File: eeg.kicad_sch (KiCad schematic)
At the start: 6 parts, among them J1 Conn_01x03, J2 Conn_01x04, U2 BMI270

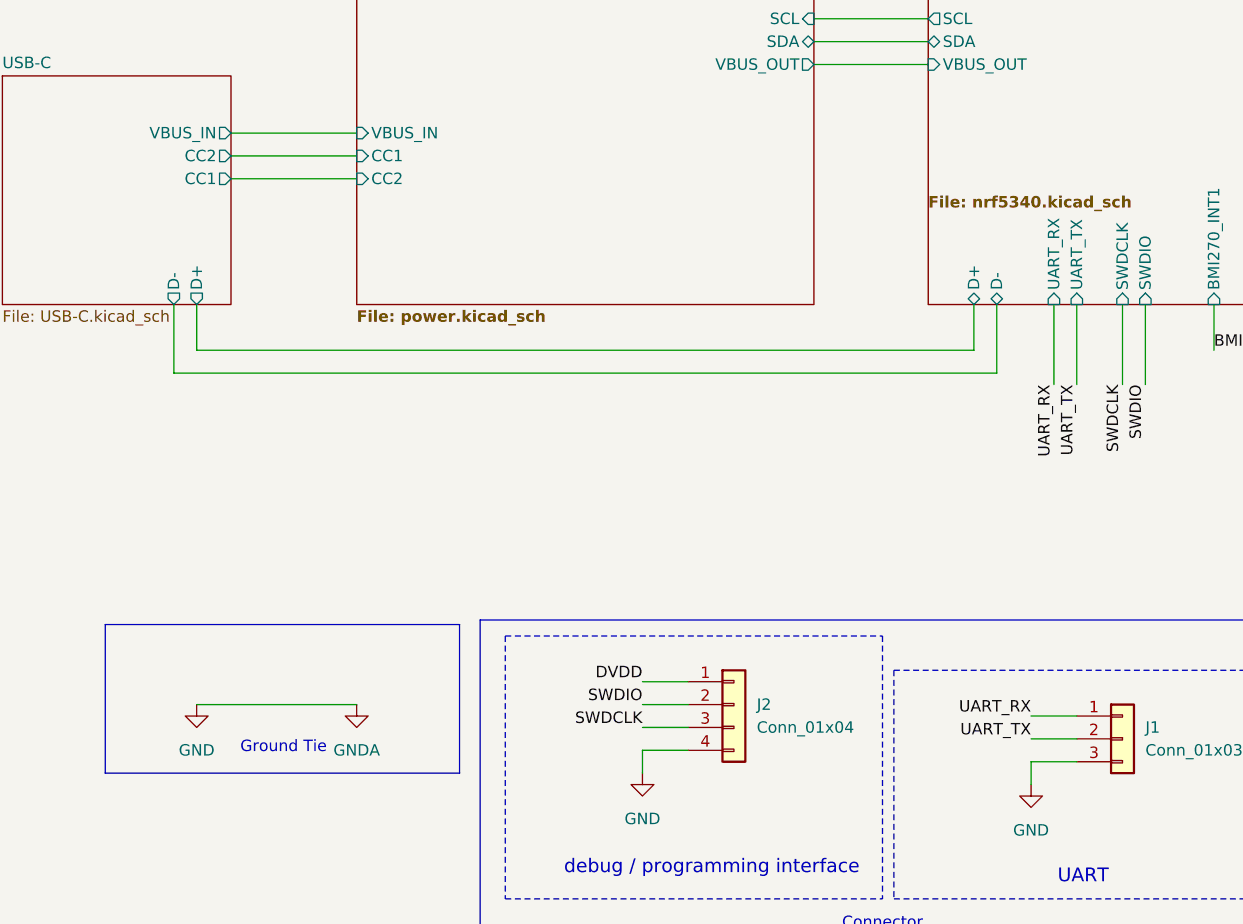
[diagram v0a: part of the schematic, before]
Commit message: Feat: 개발보드 버전으로 PCB 변경
수정사항

단가 감소
- PCB Board size up (50x50)
- blind via 제거 (전체 레이아웃 수정)
- AVDD 전력평면 추가
- ADS1299 안쓰는핀 GND
- ADS1299 배치 변경 (Layout Reference 적용)

개발보드만 적용사항
- Pin Header size up 1.27 → 2.54mm
- PCB Size 50x50(mm)
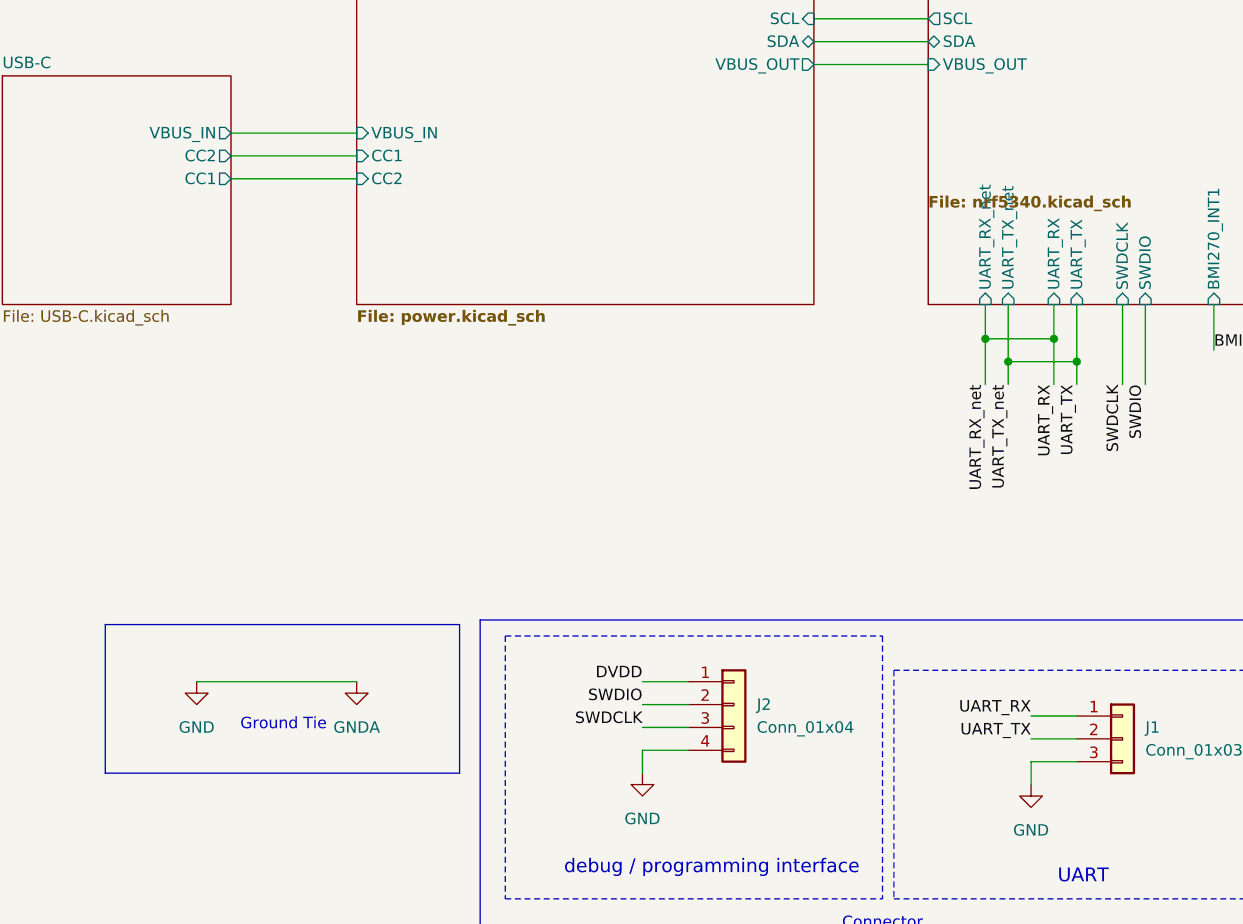
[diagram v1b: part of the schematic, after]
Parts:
- J1: footprint Connector_PinHeader_1.27mm:PinHeader_1x03_P1.27mm_Vertical -> Connector_PinHeader_2.54mm:PinHeader_1x03_P2.54mm_Vertical
- J2: footprint Connector_PinHeader_1.27mm:PinHeader_1x04_P1.27mm_Vertical -> Connector_PinHeader_2.54mm:PinHeader_1x04_P2.54mm_Vertical
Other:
- sheet USB-C ports: added none; removed D+, D-
- sheet nrf5340 ports: added UART_RX_net, UART_TX_net; removed D+, D-

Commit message: Doc: Gerber Data V0.2(dev)
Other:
- sheet nrf5340 ports: added none; removed UART_RX_net, UART_TX_net
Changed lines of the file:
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@@
 	(paper "A4")
-	(junction
-		(at 158.75 95.25)
-		(diameter 0)
-		(color 0 0 0 0)
-	)
 	(junction
 		(at 254 114.3)
@@
 	)
 	(junction
-		(at 168.91 97.79)
-		(diameter 0)
-		(color 0 0 0 0)
-	)
-	(junction
 		(at 266.7 111.76)
 		(diameter 0)
@@
 	)
 	(junction
-		(at 161.29 97.79)
-		(diameter 0)
-		(color 0 0 0 0)
-	)
-	(junction
-		(at 166.37 95.25)
-		(diameter 0)
-		(color 0 0 0 0)
-	)
-	(junction
 		(at 255.27 147.32)
 		(diameter 0)
@@
 		)
 	)
-	(wire
-		(pts
-			(xy 161.29 97.79) (xy 168.91 97.79)
-		)
-		(stroke
-			(width 0)
-			(type default)
-		)
-	)
-	(wire
-		(pts
-			(xy 158.75 100.33) (xy 158.75 95.25)
-		)
-		(stroke
-			(width 0)
-			(type default)
-		)
-	)
 	(polyline
 		(pts
@@
 	(wire
 		(pts
-			(xy 168.91 97.79) (xy 168.91 100.33)
-		)
-		(stroke
-			(width 0)
-			(type default)
-		)
-	)
-	(wire
-		(pts
 			(xy 176.53 91.44) (xy 176.53 100.33)
 		)
@@
 	(wire
 		(pts
-			(xy 161.29 100.33) (xy 161.29 97.79)
-		)
-		(stroke
-			(width 0)
-			(type default)
-		)
-	)
-	(wire
-		(pts
 			(xy 210.82 82.55) (xy 215.9 82.55)
 		)
@@
 	(wire
 		(pts
-			(xy 158.75 95.25) (xy 166.37 95.25)
-		)
-		(stroke
-			(width 0)
-			(type default)
-		)
-	)
-	(wire
-		(pts
 			(xy 240.03 36.83) (xy 240.03 40.64)
 		)
@@
 	(wire
 		(pts
-			(xy 166.37 95.25) (xy 166.37 100.33)
-		)
-		(stroke
-			(width 0)
-			(type default)
-		)
-	)
-	(wire
-		(pts
 			(xy 266.7 125.73) (xy 266.7 127)
 		)
@@
 	(wire
 		(pts
-			(xy 158.75 95.25) (xy 158.75 91.44)
-		)
-		(stroke
-			(width 0)
-			(type default)
-		)
-	)
-	(wire
-		(pts
 			(xy 74.93 77.47) (xy 88.9 77.47)
 		)
@@
 	(wire
 		(pts
-			(xy 168.91 91.44) (xy 168.91 97.79)
+			(xy 168.91 91.44) (xy 168.91 100.33)
 		)
 		(stroke
@@
 	(wire
 		(pts
-			(xy 161.29 97.79) (xy 161.29 91.44)
-		)
-		(stroke
-			(width 0)
-			(type default)
-		)
-	)
-	(wire
-		(pts
 			(xy 130.81 35.56) (xy 130.81 40.64)
 		)
@@
 	(wire
 		(pts
-			(xy 166.37 91.44) (xy 166.37 95.25)
+			(xy 166.37 91.44) (xy 166.37 100.33)
 		)
 		(stroke
@@
 		)
 	)
-	(label "UART_TX_net"
-		(at 161.29 100.33 270)
+	(label "SWDCLK"
+		(at 120.65 138.43 180)
 		(fields_autoplaced yes)
 		(effects
@@
 		)
 	)
-	(label "SWDCLK"
-		(at 120.65 138.43 180)
+	(label "AVDD"
+		(at 240.03 36.83 90)
 		(fields_autoplaced yes)
 		(effects
@@
 				(size 1.27 1.27)
 			)
-			(justify right bottom)
-		)
-	)
-	(label "AVDD"
-		(at 240.03 36.83 90)
+			(justify left bottom)
+		)
+	)
+	(label "SWDCLK"
+		(at 173.99 100.33 270)
 		(fields_autoplaced yes)
 		(effects
@@
 				(size 1.27 1.27)
 			)
-			(justify left bottom)
-		)
-	)
-	(label "SWDCLK"
-		(at 173.99 100.33 270)
+			(justify right bottom)
+		)
+	)
+	(label "DVDD"
+		(at 237.49 36.83 90)
 		(fields_autoplaced yes)
 		(effects
@@
 				(size 1.27 1.27)
 			)
-			(justify right bottom)
-		)
-	)
-	(label "DVDD"
-		(at 237.49 36.83 90)
+			(justify left bottom)
+		)
+	)
+	(label "BMI270_INT1"
+		(at 184.15 96.52 0)
 		(fields_autoplaced yes)
 		(effects
@@
 		)
 	)
-	(label "BMI270_INT1"
-		(at 184.15 96.52 0)
+	(label "UART_TX"
+		(at 168.91 100.33 270)
 		(fields_autoplaced yes)
 		(effects
@@
 				(size 1.27 1.27)
 			)
-			(justify left bottom)
-		)
-	)
-	(label "UART_TX"
-		(at 168.91 100.33 270)
+			(justify right bottom)
+		)
+	)
+	(label "SWDIO"
+		(at 120.65 135.89 180)
 		(fields_autoplaced yes)
 		(effects
@@
 		)
 	)
-	(label "SWDIO"
-		(at 120.65 135.89 180)
+	(label "DVDD"
+		(at 273.05 111.76 0)
 		(fields_autoplaced yes)
 		(effects
@@
 				(size 1.27 1.27)
 			)
-			(justify right bottom)
-		)
-	)
-	(label "DVDD"
-		(at 273.05 111.76 0)
-		(fields_autoplaced yes)
-		(effects
-			(font
-				(size 1.27 1.27)
-			)
 			(justify left bottom)
 		)
@@
 	(label "DVDD"
 		(at 120.65 133.35 180)
-		(fields_autoplaced yes)
-		(effects
-			(font
-				(size 1.27 1.27)
-			)
-			(justify right bottom)
-		)
-	)
-	(label "UART_RX_net"
-		(at 158.75 100.33 270)
 		(fields_autoplaced yes)
 		(effects
@@
 			)
 		)
-		(pin "UART_TX_net" input
-			(at 161.29 91.44 270)
-			(effects
-				(font
-					(size 1.27 1.27)
-				)
-				(justify left)
-			)
-		)
-		(pin "UART_RX_net" input
-			(at 158.75 91.44 270)
-			(effects
-				(font
-					(size 1.27 1.27)
-				)
-				(justify left)
-			)
-		)
